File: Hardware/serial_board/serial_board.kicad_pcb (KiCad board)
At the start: 2 copper layers, 80.8 x 60.1 mm, 16 parts, among them J1 Conn_01x40, J2 Conn_01x06, U1 W65C51NxP, X1 CXO_DIP8

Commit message: update serial board
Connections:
- net Net-(D1-Pad2) renamed /TX
- net Net-(D2-Pad2) renamed /RX
- net Net-(J2-Pad5) renamed /~RTS~
- J2 pad 1: Net-(J2-Pad1) -> /~DSR~
- U1 pad 11: Net-(J2-Pad1) -> GND
- U1 pad 17: GND -> /~DSR~
- U1 pad 9: Net-(U1-Pad9) -> GND
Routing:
- net Net-(J2-Pad1): track 51.5 -> 0.00 mm
- net /~DSR~: track 0.00 -> 41.7 mm
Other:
- board text added: "~DSR~"
- board text added: "~RTS~"
- board text removed: "CTS"
- board text removed: "DTR"

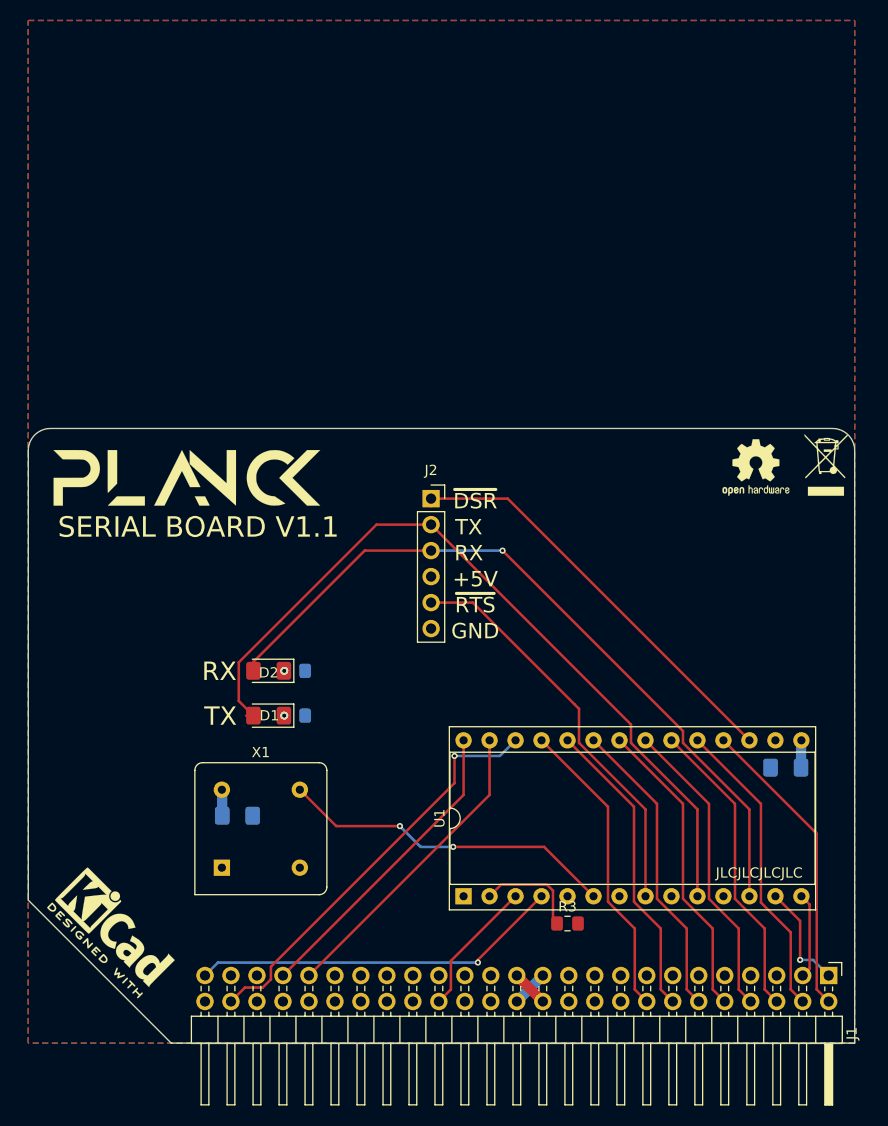
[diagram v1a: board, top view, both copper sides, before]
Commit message: Update serial board with through hole components
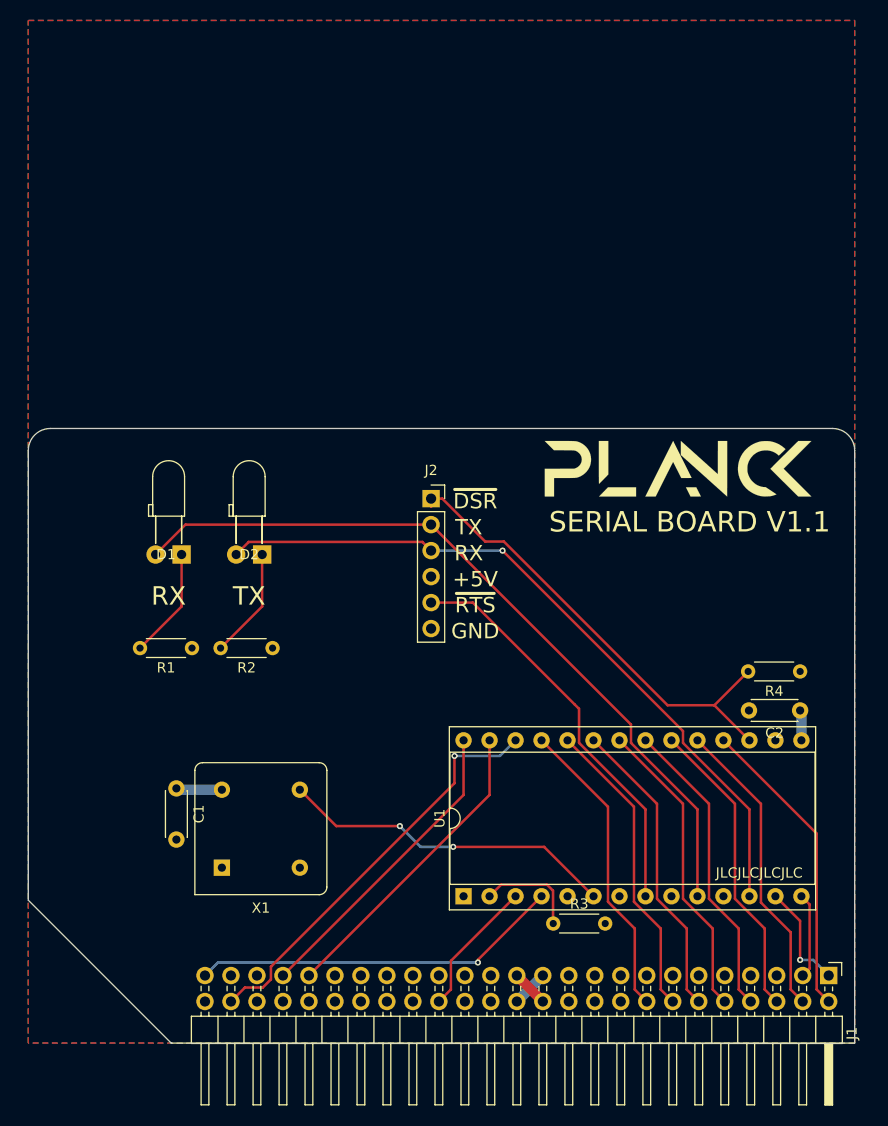
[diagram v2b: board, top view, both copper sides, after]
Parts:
- removed the G*** at (66.0, -56.0)
- removed the G*** at (15.5, -55.2)
- removed REF**: OSHW-Logo2_7.3x6mm_SilkScreen, Symbol:OSHW-Logo2_7.3x6mm_SilkScreen
- removed REF**: WEEE-Logo_4.2x6mm_SilkScreen, Symbol:WEEE-Logo_4.2x6mm_SilkScreen
- removed REF**: KiCad-Logo2_5mm_SilkScreen, Symbol:KiCad-Logo2_5mm_SilkScreen
- added G***: LOGO, Logo:logo, B.Cu at (66.3, -55.9)
- added G***: LOGO, Logo:logo, F.Cu at (63.5, -56.1)
- added R4: 10k, Resistor_THT:R_Axial_DIN0204_L3.6mm_D1.6mm_P5.08mm_Horizontal, F.Cu at (75.4, -36.3)
- C1, C2: footprint Capacitor_SMD:C_1206_3216Metric_Pad1.42x1.75mm_HandSolder -> Capacitor_THT:C_Disc_D4.3mm_W1.9mm_P5.00mm; moved to F.Cu
- D1, D2: footprint LED_SMD:LED_1206_3216Metric_Pad1.42x1.75mm_HandSolder -> LED_THT:LED_D3.0mm_Horizontal_O3.81mm_Z2.0mm
- R1, R2: value R_Small -> 330R; footprint Resistor_SMD:R_0805_2012Metric_Pad1.15x1.40mm_HandSolder -> Resistor_THT:R_Axial_DIN0204_L3.6mm_D1.6mm_P5.08mm_Horizontal; moved to F.Cu
- R3: footprint Resistor_SMD:R_0805_2012Metric_Pad1.15x1.40mm_HandSolder -> Resistor_THT:R_Axial_DIN0204_L3.6mm_D1.6mm_P5.08mm_Horizontal
- moved D1 17.9 mm to (15.0, -47.8)
- moved R1 12.0 mm to (16.0, -38.6)
- moved D2 11.4 mm to (22.9, -47.8)
- moved C1 6.54 mm to (14.5, -24.9), turned to 270 degrees
- moved C2 5.76 mm to (75.4, -32.5)
- moved R2 3.10 mm to (23.9, -38.6)
- moved R3 1.40 mm to (51.3, -11.7)
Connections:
- U1 pad 11: GND -> /~DTR~
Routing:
- net Net-(D2-Pad1): track 0.00 -> 10.8 mm, vias 1 -> 0
- net Net-(D1-Pad1): track 0.00 -> 10.8 mm, vias 1 -> 0
- net /~DSR~: track 41.7 -> 46.4 mm
- net /RX: track 73.6 -> 70.7 mm
- net +5V: track 8.83 -> 11.1 mm
- net /TX: track 78.0 -> 76.1 mm

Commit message: update gerbers for serial board
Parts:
- D1, D2: footprint LED_THT:LED_D3.0mm_Horizontal_O3.81mm_Z2.0mm -> LED_THT:LED_D3.0mm
- moved G*** 0.36 mm to (63.2, -55.9)

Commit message: update gerbers
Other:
- rule pad_to_mask_clearance: 0.05 -> 0

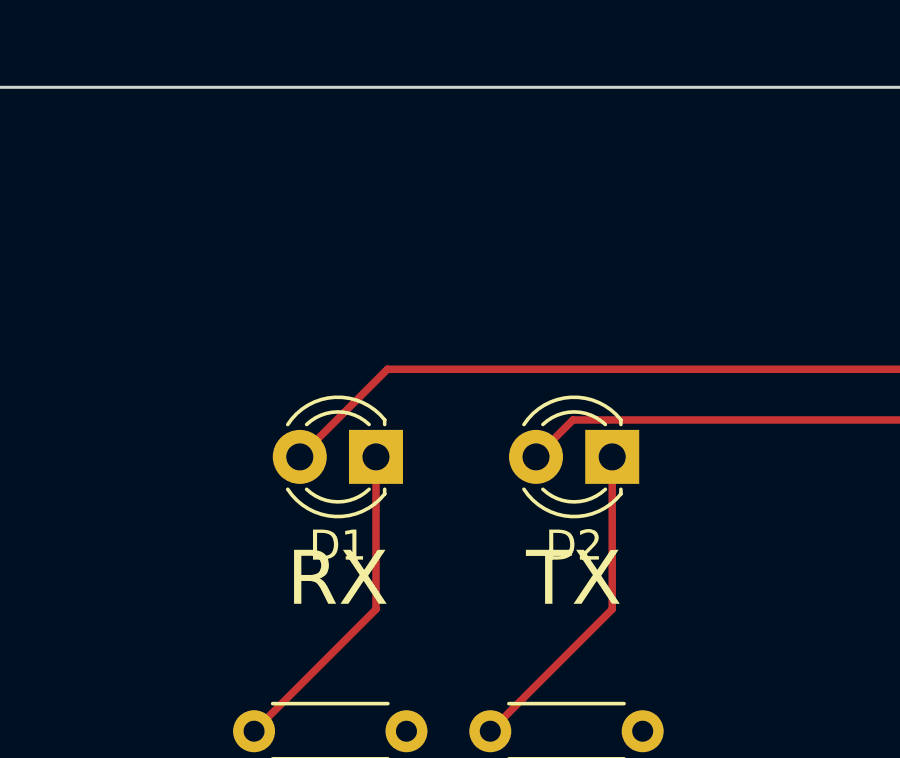
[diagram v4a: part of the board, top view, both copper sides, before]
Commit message: vertical leds
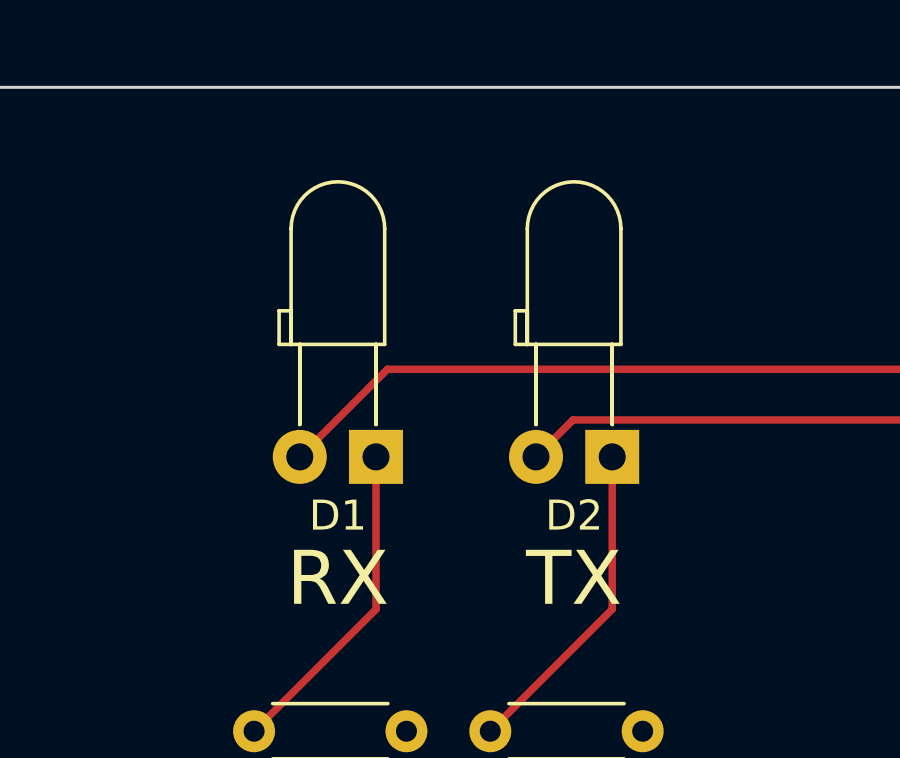
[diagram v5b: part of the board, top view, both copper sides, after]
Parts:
- D1, D2: footprint LED_THT:LED_D3.0mm -> LED_THT:LED_D3.0mm_Horizontal_O3.81mm_Z2.0mm
- moved G*** 0.25 mm to (66.0, -55.9)
